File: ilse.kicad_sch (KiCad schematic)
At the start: 91 parts, among them J1 OUT, J2 EURO RACK POWER, J3 CV Inputs, J4 1V/Oct, J5 Gate, J6 Cutoff, J7 Filter In, Q1 BC559, Q2 BC559, Q3 BC559, Q4 BC548, Q5 BC548, Q6 BC548, SW2 LFO to Filter / Freq CV, SW3 Resonance L/H, U1 TL074, U2 TL074

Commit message: layout remake in process
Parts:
- BT1, BT2: value 100 -> 9 V
- C1, C10, C11, C2, C3, C4, C5, C6, C7, C8, C9: footprint Capacitor_THT:C_Rect_L7.2mm_W2.5mm_P5.00mm_FKS2_FKP2_MKS2_MKP2 -> hybrid:C_Disc_(hybrid SMD-THT)_P5.00mm-0604; symbol ilse-rescue:C_Small-Device -> Device:C_Small
- D3, D4, D5: footprint Diode_THT:D_DO-41_SOD81_P10.16mm_Horizontal -> Diode_THT:D_DO-35_SOD27_P7.62mm_Horizontal
- Q1, Q2, Q3: symbol ilse-rescue:BC560-Transistor_BJT -> Device:Q_PNP_CBE
- R1, R10, R11, R12, R13, R14, R15, R16, R17, R18, R19, R2, R20, R21, R22, R23, R24, R25, R26, R27, R28, R29, R3, R30, R31, R32, R33, R34, R35, R36, R37, R38, R39, R4, R40, R5, R6, R7, R8, R9: symbol ilse-rescue:R_Small_US-Device -> Device:R
- RV1, RV2, RV4, RV5, RV6, RV7, RV8: symbol ilse-rescue:R_POT_US-Device -> Device:R_Potentiometer_MountingPin
- U1, U2: footprint Package_DIP:DIP-14_W7.62mm_Socket_LongPads -> Package_DIP:DIP-14_W7.62mm
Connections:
- net GND: now also RV1.MP (MountPin), RV2.MP (MountPin), RV4.MP (MountPin), RV5.MP (MountPin), RV6.MP (MountPin), RV7.MP (MountPin), RV8.MP (MountPin)
- no-connect marks 0 -> 2
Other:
- moved on the sheet: D1, RV1, RV2, RV4, RV5, RV6, RV7, RV8, U2C

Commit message: layout remake in process
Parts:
- removed H1, H2, H3, H4: MountingHole, 4ms-footprints:Rail-mount-slot, symbol ilse-rescue:MountingHole-Mechanical
- added unit 2 of SW2
- BT1, BT2: symbol ilse-rescue:Battery_Cell-Device -> Device:Battery_Cell
- C12, C13: symbol ilse-rescue:CP_Small-Device -> Device:C_Polarized_Small
- D1, D2: symbol ilse-rescue:LED-Device -> Device:LED
- J1, J4, J5, J6, J7: symbol ilse-rescue:AudioJack2_SwitchT-Connector -> Connector:AudioJack2_SwitchT
- J2: symbol ilse-rescue:EURO_PWR_2x5-eurocad -> CHAIR:EURO_PWR_2x5-Eurorack
- J3: symbol ilse-rescue:Conn_01x06-Connector_Generic -> Connector_Generic:Conn_01x06
- JP1: symbol ilse-rescue:Jumper_NO_Small-Device -> Jumper:Jumper_2_Open
- LOGO1: symbol ilse-rescue:CHAIR-LOGO-chair -> CHAIR:CHAIR-LOGO
- Q4, Q5, Q6: symbol ilse-rescue:BC550-Transistor_BJT -> Transistor_BJT:BC550
- RV3: symbol ilse-rescue:R_POT_TRIM-Device -> Device:R_Potentiometer_Trim
- SW1: renamed from SW2; footprint CHAIR:Switch_DPDT_PVA2 -> hybrid:Switch_DPDT_(Hybrid Miniature-SubMiniature); symbol CHAIR:SW_DPDT_x2-Switch-PVA2 -> Switch:SW_DPDT_x2
- SW2: renamed from SW3; value Resonance L/H -> Resonance; footprint CHAIR:Switch_DPDT_PVA2 -> hybrid:Switch_DPDT_(Hybrid Miniature-SubMiniature); symbol CHAIR:SW_DPDT_x2-Switch-PVA2 -> Switch:SW_DPDT_x2
- U1, U2: symbol ilse-rescue:TL074-Amplifier_Operational -> Amplifier_Operational:TL074
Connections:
- net at C8.1, R22.1, R23.1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: now also SW2.5 (B)
- net at C10.1, SW2.1 (A): now also SW2.4 (A)
- net at SW1.4 (A): now also C7.2, Q6.2 (B), SW1.3 (C), U2.13 (-), U2.8
- now unconnected: SW1.6 (A)
- no-connect marks 2 -> 3
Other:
- moved on the sheet: C10, C3, C4, Q3, Q5, R1, R10, R11, R13, R14, R15, R16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

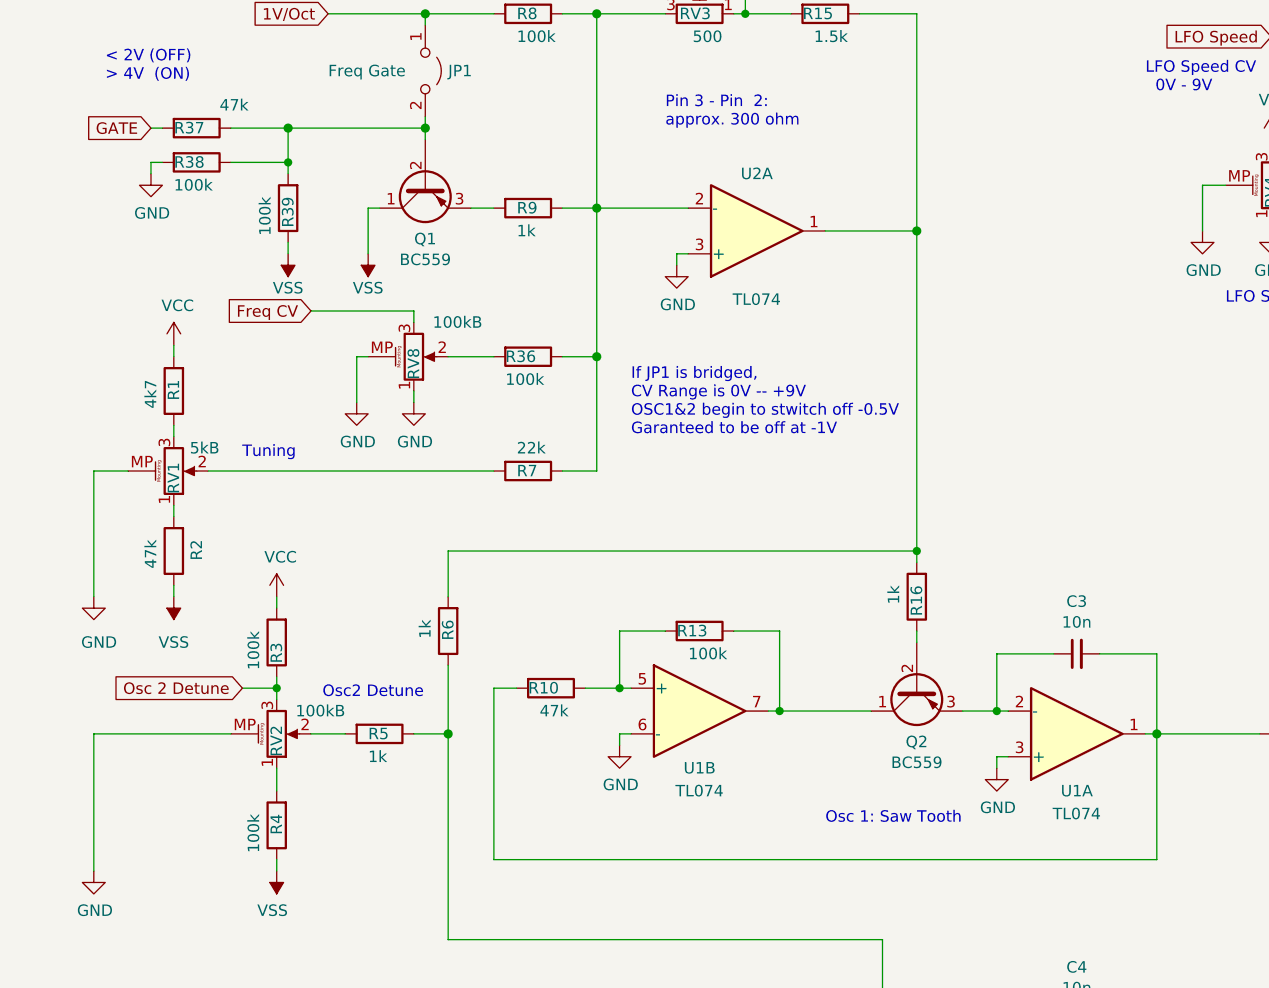
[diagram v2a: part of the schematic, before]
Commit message: finished routing and squashed DRC errors down to 0
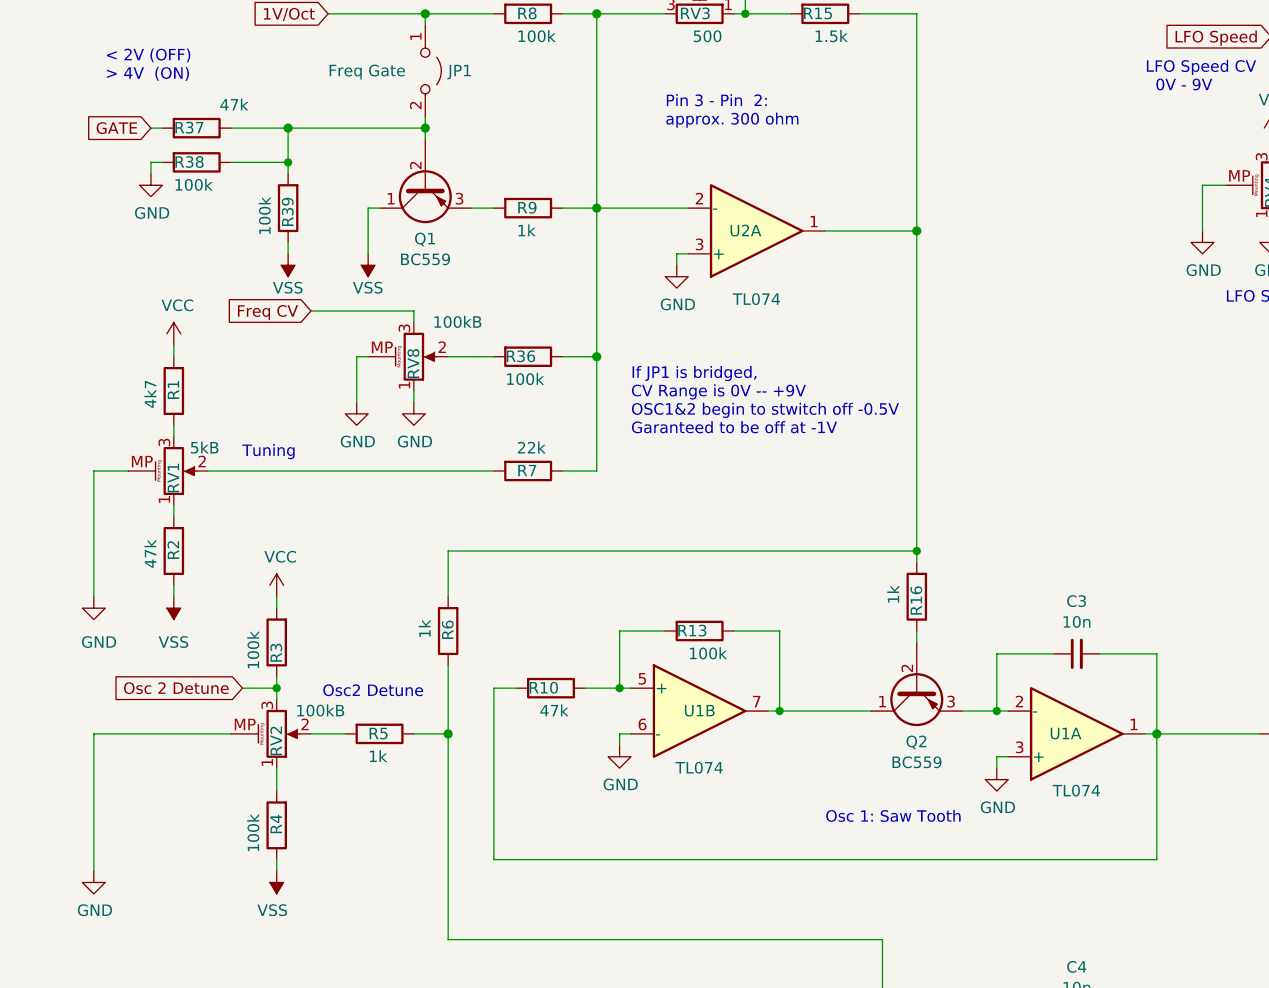
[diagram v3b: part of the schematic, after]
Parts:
- Q1, Q2, Q3, Q4, Q5, Q6: footprint Package_TO_SOT_THT:TO-92_Inline -> Package_TO_SOT_THT:TO-92_Inline_Wide
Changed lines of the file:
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@@
   (symbol (lib_id "Amplifier_Operational:TL074") (at 130.81 97.79 0) (mirror x) (unit 1)
     (in_bom yes) (on_board yes)
-    (property "Reference" "U1" (id 0) (at 130.81 104.14 0))
-    (property "Value" "TL074" (id 1) (at 130.81 106.68 0))
+    (property "Reference" "U1" (id 0) (at 129.54 97.79 0))
+    (property "Value" "TL074" (id 1) (at 130.81 104.14 0))
     (property "Footprint" "Package_DIP:DIP-14_W7.62mm" (id 2) (at 125.73 96.52 0)
       (effects (font (size 1.27 1.27)) hide)
@@
       (effects (font (size 1.27 1.27)) (justify left))
     )
-    (property "Footprint" "Package_TO_SOT_THT:TO-92_Inline" (id 2) (at 194.31 92.075 0)
+    (property "Footprint" "Package_TO_SOT_THT:TO-92_Inline_Wide" (id 2) (at 194.31 92.075 0)
       (effects (font (size 1.27 1.27) italic) (justify left) hide)
     )
@@
     (property "Reference" "Q2" (id 0) (at 113.03 98.679 90))
     (property "Value" "BC559" (id 1) (at 113.03 100.9904 90))
-    (property "Footprint" "Package_TO_SOT_THT:TO-92_Inline" (id 2) (at 110.49 97.79 0)
+    (property "Footprint" "Package_TO_SOT_THT:TO-92_Inline_Wide" (id 2) (at 110.49 97.79 0)
       (effects (font (size 1.27 1.27)) hide)
     )
@@
   (symbol (lib_id "Device:R") (at 30.48 77.47 180) (unit 1)
     (in_bom yes) (on_board yes)
-    (property "Reference" "R2" (id 0) (at 33.02 76.2 90)
+    (property "Reference" "R2" (id 0) (at 30.48 76.2 90)
       (effects (font (size 1.27 1.27)) (justify left))
     )
@@
     (property "Reference" "Q3" (id 0) (at 109.22 143.129 90))
     (property "Value" "BC559" (id 1) (at 109.22 145.4404 90))
-    (property "Footprint" "Package_TO_SOT_THT:TO-92_Inline" (id 2) (at 106.68 142.24 0)
+    (property "Footprint" "Package_TO_SOT_THT:TO-92_Inline_Wide" (id 2) (at 106.68 142.24 0)
       (effects (font (size 1.27 1.27)) hide)
     )
@@
       (effects (font (size 1.27 1.27)) (justify left))
     )
-    (property "Footprint" "Package_TO_SOT_THT:TO-92_Inline" (id 2) (at 175.26 59.055 0)
+    (property "Footprint" "Package_TO_SOT_THT:TO-92_Inline_Wide" (id 2) (at 175.26 59.055 0)
       (effects (font (size 1.27 1.27) italic) (justify left) hide)
     )
@@
     (property "Reference" "Q1" (id 0) (at 58.42 42.799 90))
     (property "Value" "BC559" (id 1) (at 58.42 45.1104 90))
-    (property "Footprint" "Package_TO_SOT_THT:TO-92_Inline" (id 2) (at 55.88 41.91 0)
+    (property "Footprint" "Package_TO_SOT_THT:TO-92_Inline_Wide" (id 2) (at 55.88 41.91 0)
       (effects (font (size 1.27 1.27)) hide)
     )
@@
       (effects (font (size 1.27 1.27)) (justify left))
     )
-    (property "Footprint" "Package_TO_SOT_THT:TO-92_Inline" (id 2) (at 261.62 40.005 0)
+    (property "Footprint" "Package_TO_SOT_THT:TO-92_Inline_Wide" (id 2) (at 261.62 40.005 0)
       (effects (font (size 1.27 1.27) italic) (justify left) hide)
     )
@@
   (symbol (lib_id "Amplifier_Operational:TL074") (at 88.9 95.25 0) (unit 2)
     (in_bom yes) (on_board yes)
-    (property "Reference" "U1" (id 0) (at 88.9 101.6 0))
-    (property "Value" "TL074" (id 1) (at 88.9 104.14 0))
+    (property "Reference" "U1" (id 0) (at 88.9 95.25 0))
+    (property "Value" "TL074" (id 1) (at 88.9 101.6 0))
     (property "Footprint" "Package_DIP:DIP-14_W7.62mm" (id 2) (at 83.82 96.52 0)
       (effects (font (size 1.27 1.27)) hide)
@@
   (symbol (lib_id "Amplifier_Operational:TL074") (at 95.25 41.91 0) (mirror x) (unit 1)
     (in_bom yes) (on_board yes)
-    (property "Reference" "U2" (id 0) (at 95.25 35.56 0))
+    (property "Reference" "U2" (id 0) (at 93.98 41.91 0))
     (property "Value" "TL074" (id 1) (at 95.25 49.53 0))
     (property "Footprint" "Package_DIP:DIP-14_W7.62mm" (id 2) (at 90.17 40.64 0)
@@
     )
     (path "/00000000-0000-0000-0000-00005dbc3bae"
-      (reference "Q1") (unit 1) (value "BC559") (footprint "Package_TO_SOT_THT:TO-92_Inline")
+      (reference "Q1") (unit 1) (value "BC559") (footprint "Package_TO_SOT_THT:TO-92_Inline_Wide")
     )
     (path "/00000000-0000-0000-0000-00005db0d9c5"
-      (reference "Q2") (unit 1) (value "BC559") (footprint "Package_TO_SOT_THT:TO-92_Inline")
+      (reference "Q2") (unit 1) (value "BC559") (footprint "Package_TO_SOT_THT:TO-92_Inline_Wide")
     )
     (path "/00000000-0000-0000-0000-00005db4d06d"
-      (reference "Q3") (unit 1) (value "BC559") (footprint "Package_TO_SOT_THT:TO-92_Inline")
+      (reference "Q3") (unit 1) (value "BC559") (footprint "Package_TO_SOT_THT:TO-92_Inline_Wide")
     )
     (path "/00000000-0000-0000-0000-00005db96bf3"
-      (reference "Q4") (unit 1) (value "BC548") (footprint "Package_TO_SOT_THT:TO-92_Inline")
+      (reference "Q4") (unit 1) (value "BC548") (footprint "Package_TO_SOT_THT:TO-92_Inline_Wide")
     )
     (path "/00000000-0000-0000-0000-00005da5aea7"
-      (reference "Q5") (unit 1) (value "BC548") (footprint "Package_TO_SOT_THT:TO-92_Inline")
+      (reference "Q5") (unit 1) (value "BC548") (footprint "Package_TO_SOT_THT:TO-92_Inline_Wide")
     )
     (path "/00000000-0000-0000-0000-00005dbd2099"
-      (reference "Q6") (unit 1) (value "BC548") (footprint "Package_TO_SOT_THT:TO-92_Inline")
+      (reference "Q6") (unit 1) (value "BC548") (footprint "Package_TO_SOT_THT:TO-92_Inline_Wide")
     )
     (path "/00000000-0000-0000-0000-00005db3ee8d"
